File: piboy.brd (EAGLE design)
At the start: 76.2 x 76.2 mm, 71 parts, among them CN4 MicroUSB, T1 MMUN2133LT1G, U1 TPS61090RSAR, U2 MCP73871

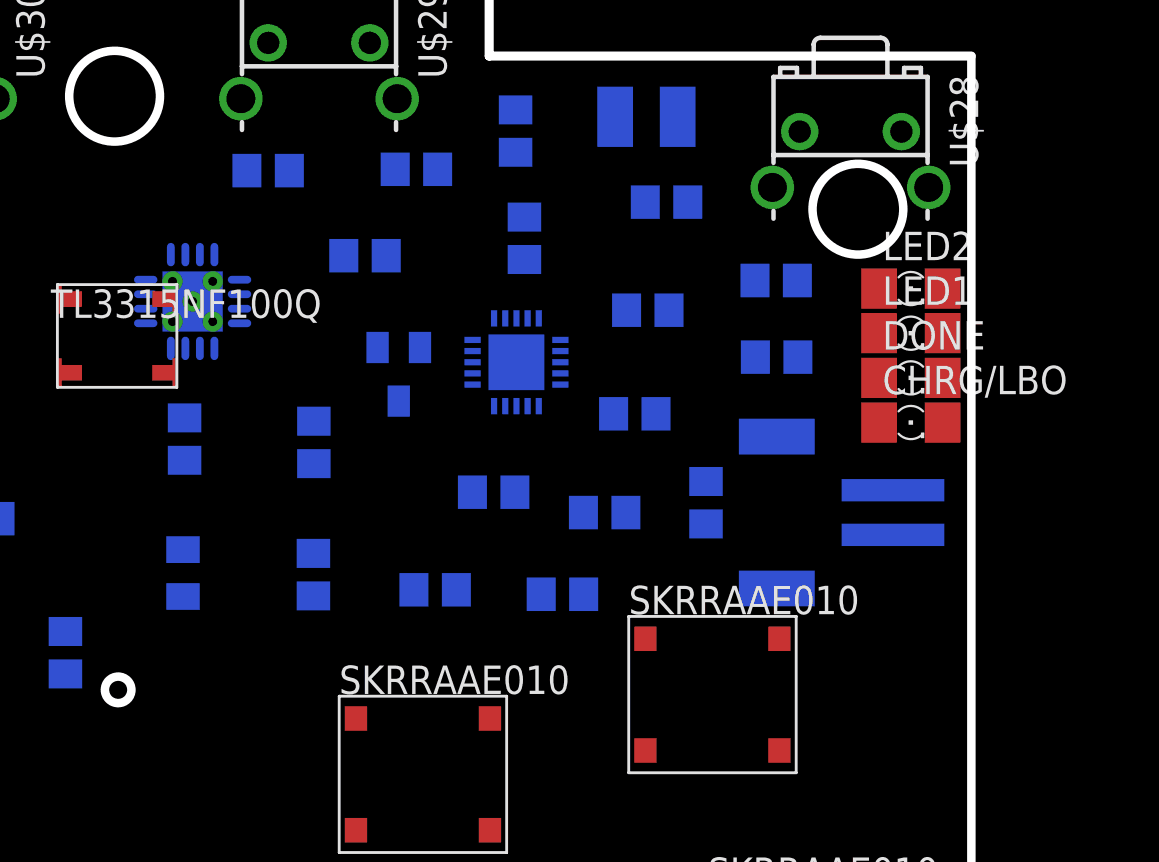
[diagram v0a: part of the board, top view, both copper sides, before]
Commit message: -added traces -performed a DRC, no overlaps found
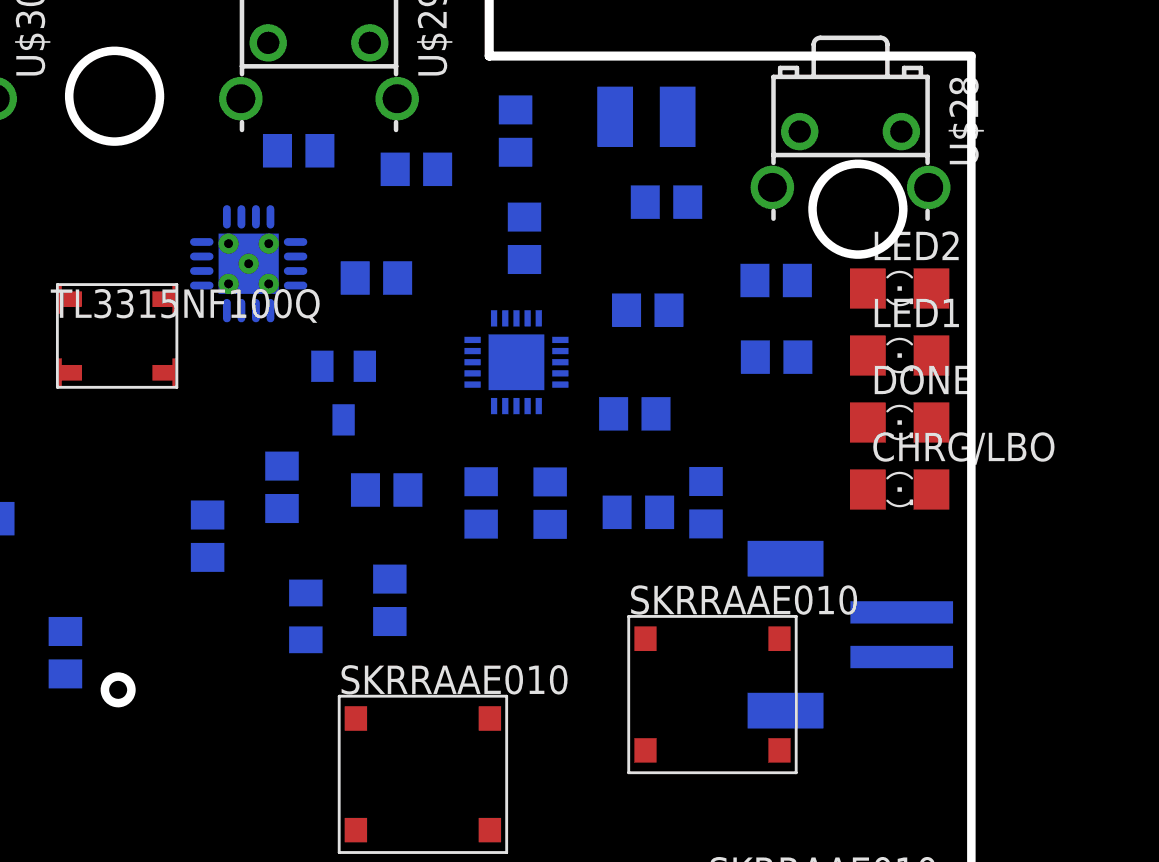
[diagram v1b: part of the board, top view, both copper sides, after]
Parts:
- moved C4 5.83 mm to (46.4, 47.3)
- moved B1 5.48 mm to (69.4, 46.5)
- moved R2 4.79 mm to (50.0, 53.0)
- moved R13 4.47 mm to (42.0, 50.9)
- moved R16 4.40 mm to (54.3, 52.4), turned to 90 degrees
- moved R17 4.12 mm to (57.4, 52.4), turned to 90 degrees
- moved C1 3.61 mm to (50.2, 48.0)
- moved CHRG/LBO 3.04 mm to (73.0, 53.0)
- moved U1 3.03 mm to (43.9, 63.1)
- moved T1 2.61 mm to (48.1, 57.3)
- moved R1 2.47 mm to (45.3, 53.1)
- moved DONE 2.06 mm to (73.0, 56.0)
- moved R4 1.63 mm to (46.1, 68.2)
- moved C8 1.51 mm to (61.3, 52.0)
- moved C7 1.12 mm to (49.6, 62.5)
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
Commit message: -whoops forgot to save
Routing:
- net GND: track 0.00 -> 635.0 mm, vias 0 -> 5
- net 3.3V: track 0.00 -> 123.1 mm, vias 0 -> 3
- net 5.0V: track 0.00 -> 119.7 mm, vias 0 -> 4
- net J_LFT: track 0.00 -> 110.4 mm, vias 0 -> 3
- net VBUS: track 0.00 -> 109.4 mm, vias 0 -> 6
- net VBAT: track 0.00 -> 92.8 mm, vias 0 -> 2
- net LEFT_HDPHN: track 0.00 -> 77.4 mm
- net J_X: track 0.00 -> 74.9 mm, vias 0 -> 3
- net MOSI: track 0.00 -> 72.5 mm, vias 0 -> 3
- net ENABLE: track 0.00 -> 72.1 mm, vias 0 -> 3
- net MISO: track 0.00 -> 71.1 mm, vias 0 -> 3
- net J_VDN: track 0.00 -> 66.6 mm, vias 0 -> 2
- net J_VUP: track 0.00 -> 66.4 mm, vias 0 -> 3
- net TFT_DC_3V: track 0.00 -> 62.6 mm, vias 0 -> 2
- net N$1: track 0.00 -> 60.2 mm, vias 0 -> 2
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
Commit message: -went through drc
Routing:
- net CMP_VIDEO_OUT: track 31.1 -> 55.9 mm, vias 0 -> 2
- net 3.3V: track 123.1 -> 108.9 mm, vias 3 -> 7
- net J_LFT: track 110.4 -> 119.7 mm, vias 3 -> 7
- net J_SEL: track 21.3 -> 26.2 mm
- net RIGHT_HDPHN: track 51.5 -> 53.7 mm
- net LEFT_HDPHN: track 77.4 -> 76.2 mm, vias 0 -> 4
- net RIGHT_SPEAKER: track 48.6 -> 49.4 mm
- net VBUS: track 109.4 -> 110.0 mm
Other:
- outline, holes or cut-outs redrawn

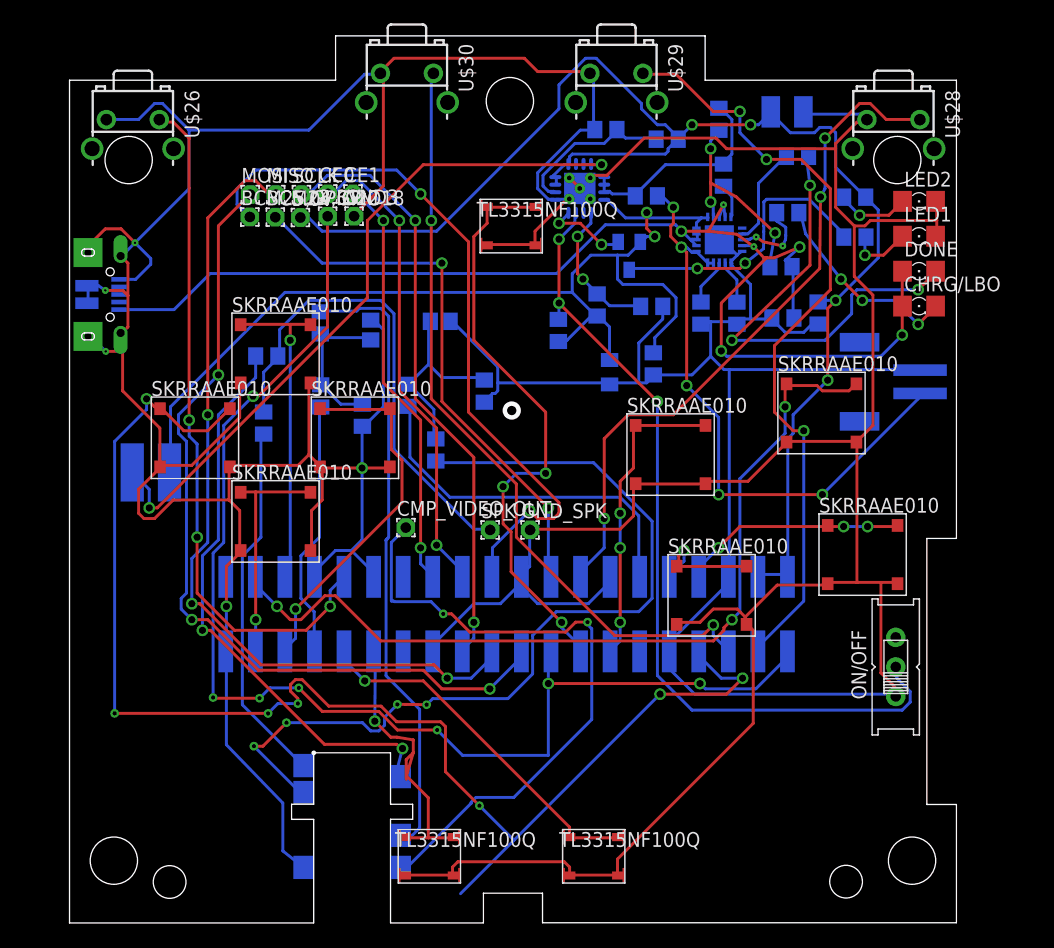
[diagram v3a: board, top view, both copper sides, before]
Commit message: TODO: edit device packages to remove silkscreen
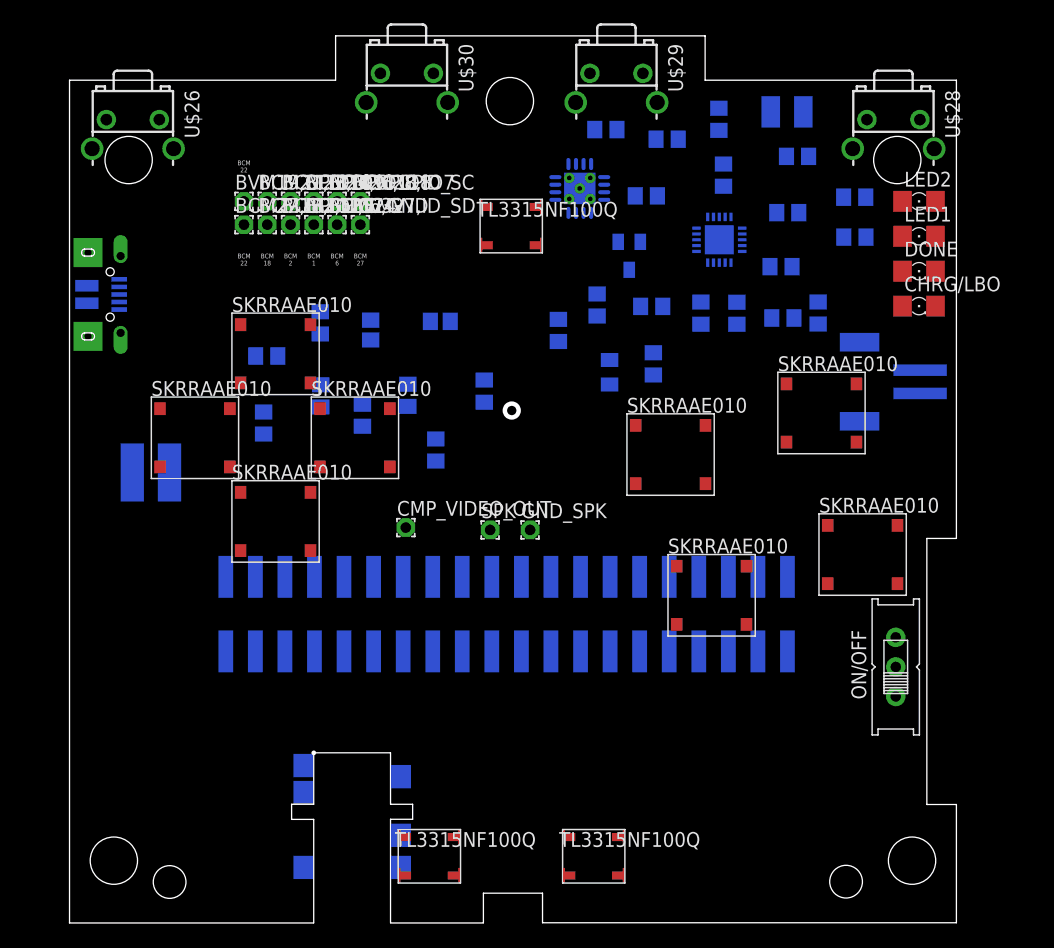
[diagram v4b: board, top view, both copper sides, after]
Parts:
- removed 3.3V, 5.0V, BCM24,GPIO18, BCM25,GPIO22, CE0, CE1, GND3, MISO, MOSI, SCLK: (no value), wirepad:1,6/0,9
- added BCM1,3.3V, BCM18,GPIO24, BCM2,5.0V, BCM21,GPIO9, BCM22,GPIO25, BCM23,GPIO11, BCM24,GPIO8, BCM26,GPIO7, BCM27,ID_SD, BCM28,ID_SC, BCM6,GND, BVM19,GPIO10: (no value), wirepad:1,6/0,9
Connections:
- removed net CE0: CE0.1, U$9.P24
- removed net CE1: CE1.1, U$9.P26
- removed net TFT_DC_3V: BCM25,GPIO22.1, U$9.P22
- new net EECLK: BCM28,ID_SC.1, U$9.P28
- new net EEDATA: BCM27,ID_SD.1, U$9.P27
- new net RT_CS: BCM26,GPIO7.1, U$9.P26
- new net TFT_CS: BCM24,GPIO8.1, U$9.P24
- new net TFT_DC: BCM22,GPIO25.1, U$9.P22
- net 3.3V: now also BCM1,3.3V.1; no longer 3.3V.1
- net 5.0V: now also BCM2,5.0V.1; no longer 5.0V.1
- net GND: now also BCM6,GND.1; no longer GND3.1
- net J_BRT: now also U$30.1, U$9.P5; no longer U$25.P1, U$25.P2, U$9.P15
- net J_VDN: now also U$25.P1, U$25.P2, U$9.P15; no longer U$30.1, U$9.P5
- net J_VUP: now also U$9.P40; no longer U$9.P3
- net MISO: now also BCM21,GPIO9.1; no longer MISO.1
- net MOSI: now also BVM19,GPIO10.1; no longer MOSI.1
- net RT_INT: now also BCM18,GPIO24.1; no longer BCM24,GPIO18.1
- net SCLK: now also BCM23,GPIO11.1; no longer SCLK.1
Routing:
- net GND: track 635.0 -> 0.00 mm, vias 5 -> 0
- net 5.0V: track 119.7 -> 0.00 mm, vias 4 -> 0
- net J_LFT: track 119.7 -> 0.00 mm, vias 7 -> 0
- net VBUS: track 110.0 -> 0.00 mm, vias 6 -> 0
- net 3.3V: track 108.9 -> 0.00 mm, vias 7 -> 0
- net VBAT: track 92.8 -> 0.00 mm, vias 2 -> 0
- net LEFT_HDPHN: track 76.2 -> 0.00 mm, vias 4 -> 0
- net J_X: track 74.9 -> 0.00 mm, vias 3 -> 0
- net MOSI: track 72.5 -> 0.00 mm, vias 3 -> 0
- net ENABLE: track 72.1 -> 0.00 mm, vias 3 -> 0
- net MISO: track 71.1 -> 0.00 mm, vias 3 -> 0
- net J_VDN: track 66.6 -> 0.00 mm, vias 2 -> 0
- net J_VUP: track 66.4 -> 0.00 mm, vias 3 -> 0
- net TFT_DC_3V: track 62.6 -> 0.00 mm, vias 2 -> 0
- net N$1: track 60.2 -> 0.00 mm, vias 2 -> 0
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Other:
- board text added: "BCM 1"
- board text added: "BCM 18"
- board text added: "BCM 2"
- board text added: "BCM 22"
- board text added: "BCM 27"
- board text added: "BCM 6"

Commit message: -removed all problematic silkscreen -exported all parts into a new library, piboy_new.lbr TODO: Rename piboy_new.lbr
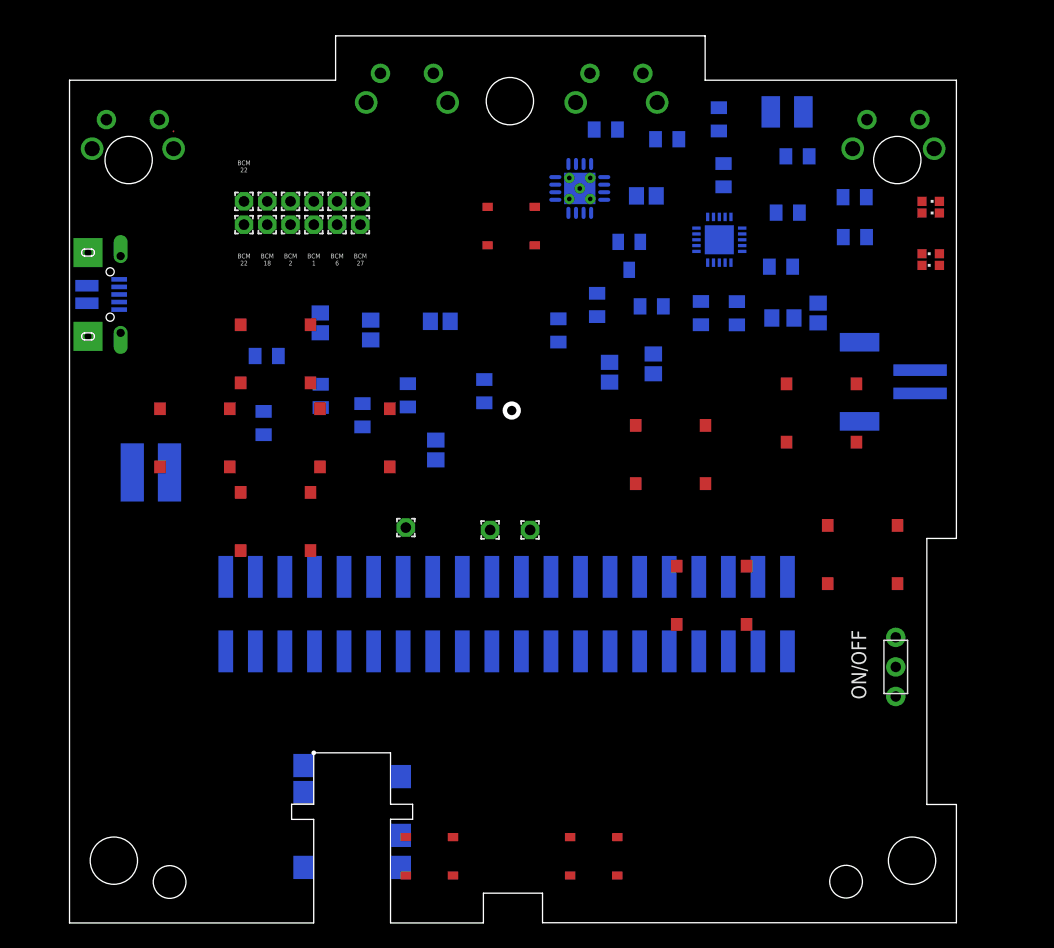
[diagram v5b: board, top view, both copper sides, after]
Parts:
- BCM1,3.3V, BCM18,GPIO24, BCM2,5.0V, BCM21,GPIO9, BCM22,GPIO25, BCM23,GPIO11, BCM24,GPIO8, BCM26,GPIO7, BCM27,ID_SD, BCM28,ID_SC, BCM6,GND, BVM19,GPIO10, CMP_VIDEO_OUT, GND_SPK, SPK: device wirepad:1,6/0,9 -> piboy_new:WIREPAD_1,6/0,9
- C1, C2, C7: device microbuilder:0805-NO -> adafruit:C0805
- C10, C5: device resistor:C0805 -> adafruit:C0805
- C4: device microbuilder:0805_10MGAP -> adafruit:C0805
- C6: device rcl:C1210 -> adafruit:C1210
- CHRG/LBO, DONE, LED1, LED2: device adafruit:1206 -> piboy_new:ADAFRUIT_CHIPLED_0603
- ON/OFF: device adafruit:EG1218 -> piboy_new:ADAFRUIT_EG1218
- R1, R10, R11, R12, R13, R14, R15, R16, R17, R18, R2, R20, R3, R4, R5, R6, R7, R8, R9, THERM: device resistor:R0805 -> adafruit:R0805
- U$26, U$28, U$29, U$30: value TL1105L-4,3 -> SWITCH_TL1105L-4,3; device switch:TL1105L-4,3 -> piboy_new:SWITCH_TL1105L-4,3
- moved CHRG/LBO 4.61 mm to (74.0, 57.5), turned to 90 degrees
- moved LED1 2.24 mm to (74.0, 61.0), turned to 270 degrees
- moved DONE 1.12 mm to (74.0, 56.5), turned to 90 degrees
- moved LED2 1.00 mm to (74.0, 62.0), turned to 270 degrees

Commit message: -redid audio circuit -moved around components on the board -began silkscreen -cleared clearance, overlap, airwire DRC -checked component values
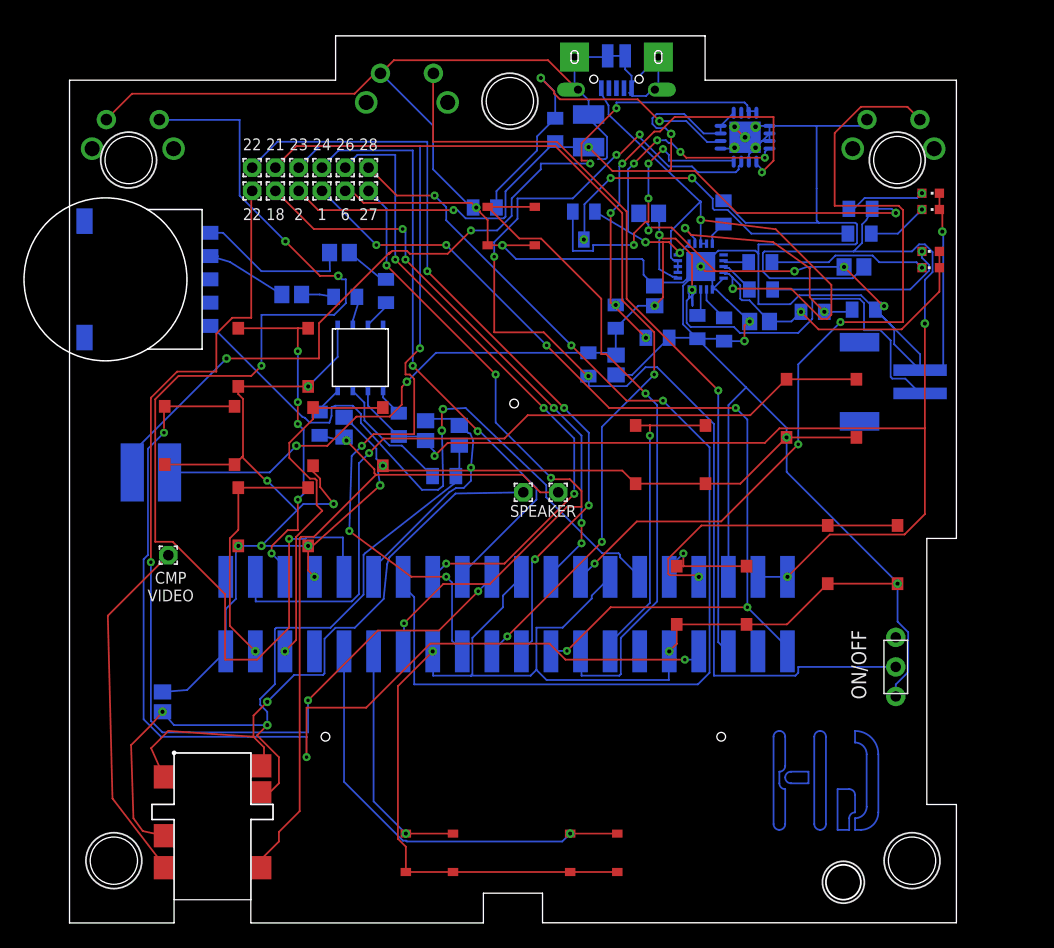
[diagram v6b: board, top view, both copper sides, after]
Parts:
- removed C10, C5: 1uF, adafruit:C0805
- removed C9: 33nF, adafruit:C0805
- removed GND_SPK, SPK: (no value), piboy_new:WIREPAD_1,6/0,9
- removed R10, R9: 270R, adafruit:R0805
- removed R11, R12: 150R, adafruit:R0805
- removed R15, R18: 10KR, adafruit:R0805
- removed U$29: SWITCH_TL1105L-4,3, piboy_new:SWITCH_TL1105L-4,3
- added C11, C12: 1uf, piboy_new:ADAFRUIT_C0805
- added C13: 10uf, piboy_new:ADAFRUIT_C0805
- added C14, C15: 220pf, piboy_new:ADAFRUIT_C0805
- added FB1, FB2: 100 Ohm @ 100 Mhz, piboy_new:ADAFRUIT_R0805
- added R19, R21: 100, piboy_new:ADAFRUIT_R0805
- added R22: 10k, piboy_new:ADAFRUIT_R0805
- added SPK1, SPK2: (no value), piboy_new:WIREPAD_1,6/0,9
- added U$33: RK10J12R0A0B, piboy_new:RK10J12R0A0B
- added U$40: SJ-43504-SMT-TR, SJ-43504-SMT-TR:SJ-43504-SMT-TR
- C3: value 33nF -> 100nf; device adafruit:C0805 -> piboy_new:ADAFRUIT_C0805
- C8: device microbuilder:0805-NO -> piboy_new:ADAFRUIT_C0805
- T1: device transistor:SC59-BEC -> piboy_new:TRANSISTOR_SC59-BEC
- U$31: value SJ-43504-SMT-TR -> PAM8302A; device SJ-43504-SMT-TR:SJ-43504-SMT-TR -> piboy_new:PAM8302A
- moved CN4 47.3 mm to (47.0, 72.5), turned to 180 degrees
- moved U$31 46.8 mm to (25.0, 48.7), turned to 180 degrees
- moved C3 40.5 mm to (8.00, 19.0), turned to 90 degrees
- moved R7 20.6 mm to (68.2, 52.7), turned to 180 degrees
- moved CMP_VIDEO_OUT 20.5 mm to (8.50, 31.6)
- moved C6 17.1 mm to (44.6, 68.1), turned to 90 degrees
- moved U1 14.9 mm to (58.0, 67.5)
- moved R4 12.4 mm to (35.7, 61.5)
- moved R3 9.65 mm to (41.7, 68.1), turned to 270 degrees
- moved R14 9.65 mm to (59.4, 56.8)
- moved C4 7.62 mm to (50.3, 53.9), turned to 90 degrees
- moved R8 6.99 mm to (59.4, 54.4)
- moved C2 5.02 mm to (67.4, 56.4), turned to 0 degrees
- moved R6 4.74 mm to (63.9, 52.5), turned to 0 degrees
- moved T1 4.69 mm to (44.2, 59.9)
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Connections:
- removed net LEFT_HDPHN: C5.2, U$31.P$2
- removed net LEFT_SPEAKER: R18.2, U$31.P$5
- removed net N$14: C10.1, C9.1, R10.2, R11.1
- removed net N$19: C3.2, C5.1, R12.1, R9.2
- removed net N$24: R15.1, R18.1, SPK.1
- removed net RIGHT_HDPHN: C10.2, U$31.P$3\
- removed net RIGHT_SPEAKER: R15.2, U$31.P$6
- new net AUD+: SPK2.1, U$40.P$5, U$40.P$6
- new net AUD-: C15.1, FB1.2, SPK1.1, U$40.P$4
- new net N$17: C12.1, R21.1
- new net N$18: R21.2, U$31.P$3
- new net N$20: C11.1, R19.1
- new net N$21: R19.2, U$31.P$2
- new net N$22: R22.2, U$31.P$5
- new net N$23: FB1.1, U$31.P$8
- new net N$25: C11.2, U$33.P$2
- new net N$26: C12.2, U$33.P$1
- new net N$27: FB2.1, U$31.P$7
- new net N$29: C14.1, C3.1, FB2.2, U$40.P$2, U$40.P$3\
- net 5.0V: now also C13.1, R22.1, U$31.P$6
- net CMP_VIDEO_OUT: now also U$40.P$1; no longer U$31.P$1
- net GND: now also C13.2, C14.2, C15.2, C3.2, U$31.P$1; no longer C3.1, C9.2, GND_SPK.1, R11.2, R12.2, U$29.2, U$31.P$4
- net J_VUP: no longer U$29.1
- net PWM0: now also U$33.P$3; no longer R9.1
- net PWM1: no longer R10.1
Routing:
- net GND: track 0.00 -> 600.7 mm, vias 0 -> 24
- net 5.0V: track 0.00 -> 197.7 mm, vias 0 -> 7
- net J_LSH: track 0.00 -> 98.1 mm, vias 0 -> 4
- net ENABLE: track 0.00 -> 97.8 mm, vias 0 -> 4
- net EECLK: track 0.00 -> 94.7 mm, vias 0 -> 3
- net J_LFT: track 0.00 -> 91.5 mm, vias 0 -> 3
- net TFT_DC: track 0.00 -> 89.0 mm, vias 0 -> 3
- net VBAT: track 0.00 -> 85.4 mm, vias 0 -> 9
- net 3.3V: track 0.00 -> 84.5 mm, vias 0 -> 6
- net VBUS: track 0.00 -> 78.4 mm, vias 0 -> 3
- net MISO: track 0.00 -> 77.6 mm, vias 0 -> 3
- net N$1: track 0.00 -> 74.6 mm, vias 0 -> 4
- net J_RSH: track 0.00 -> 71.4 mm, vias 0 -> 3
- net J_X: track 0.00 -> 68.2 mm, vias 0 -> 1
- net MOSI: track 0.00 -> 67.9 mm, vias 0 -> 4
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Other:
- outline, holes or cut-outs redrawn
- board text added: "1"
- board text added: "18"
- board text added: "2"
- board text added: "21"
- board text added: "22"
- board text added: "23"
- board text added: "24"
- board text added: "26"
- board text added: "27"
- board text added: "28"
- board text added: "6"
- board text added: "C11"
- board text added: "C12"
- board text added: "C13"
- board text added: "C14"
- board text added: "C15"
- board text added: "C3"
- board text added: "CMP VIDEO"
- board text added: "FB1"
- board text added: "FB2"
- board text added: "R19"
- board text added: "R21"
- board text added: "R22"
- board text added: "R4"
- board text added: "SPEAKER"
- board text removed: "BCM 1"
- board text removed: "BCM 18"
- board text removed: "BCM 2"
- board text removed: "BCM 22"
- board text removed: "BCM 27"
- board text removed: "BCM 6"
